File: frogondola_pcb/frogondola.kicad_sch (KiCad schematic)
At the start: 148 parts, among them J1 Conn_01x04_Pin, J10 Conn_01x01_Pin, J2 USB_C_Receptacle_USB2.0_14P, J3 Conn_01x01_Pin, J4 Conn_01x01_Pin, J5 Conn_01x01_Pin, J6 Conn_01x01_Pin, J7 Conn_01x01_Pin, J8 Conn_01x01_Pin, J9 Conn_01x01_Pin, SW1 SW_DPST_x2, SW2 SW_DPST_x2, U1 STM32F072CBTx, U2 TLV74318PDBVR, U3 XC6206PxxxMR, U4 PMW3360DM-T2QU, U5 SRV05-4

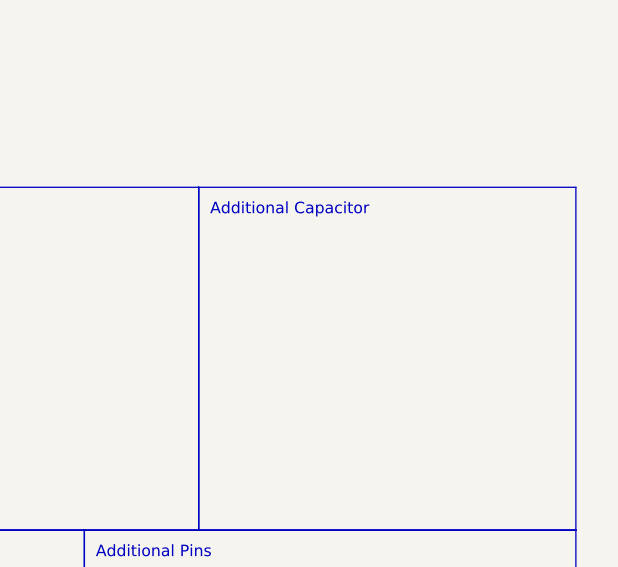
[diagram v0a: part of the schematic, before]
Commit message: Adde L60 outline footprint from https://github.com/dededecline/SST60, will update license too.
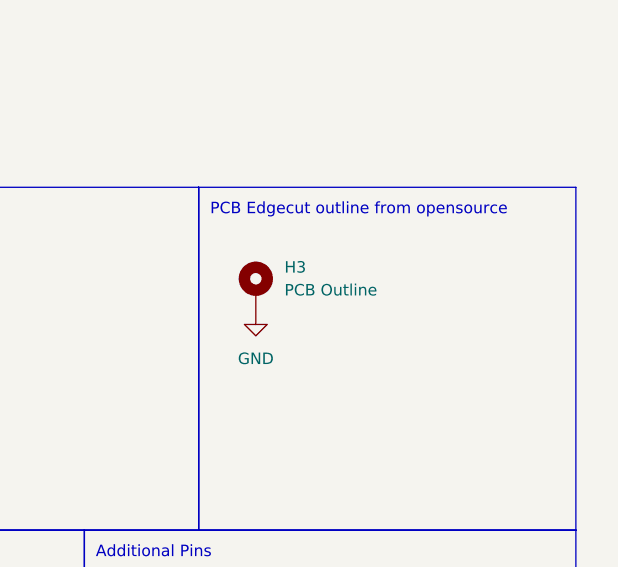
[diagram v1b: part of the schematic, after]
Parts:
- added H3: PCB Outline, pcb_outline:L60 Outline, symbol Mechanical:MountingHole_Pad
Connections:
- net GND: now also H3.1
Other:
- note added: "PCB Edgecut outline from opensource"
- note removed: "Additional Capacitor"
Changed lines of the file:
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@@
 		)
 	)
-	(text "Additional Capacitor"
+	(text "PCB Edgecut outline from opensource"
 		(exclude_from_sim no)
 		(at 367.03 63.5 0)
@@
 	)
 	(symbol
+		(lib_id "Mechanical:MountingHole_Pad")
+		(at 372.11 72.39 0)
+		(unit 1)
+		(exclude_from_sim no)
+		(in_bom yes)
+		(on_board yes)
+		(dnp no)
+		(fields_autoplaced yes)
+		(property "Reference" "H3"
+			(at 375.285 69.8499 0)
+			(effects
+				(font
+					(size 1.27 1.27)
+				)
+				(justify left)
+			)
+		)
+		(property "Value" "PCB Outline"
+			(at 375.285 72.3899 0)
+			(effects
+				(font
+					(size 1.27 1.27)
+				)
+				(justify left)
+			)
+		)
+		(property "Footprint" "pcb_outline:L60 Outline"
+			(at 372.11 72.39 0)
+			(effects
+				(font
+					(size 1.27 1.27)
+				)
+				(hide yes)
+			)
+		)
+		(property "Datasheet" "~"
+			(at 372.11 72.39 0)
+			(effects
+				(font
+					(size 1.27 1.27)
+				)
+				(hide yes)
+			)
+		)
+		(property "Description" ""
+			(at 372.11 72.39 0)
+			(effects
+				(font
+					(size 1.27 1.27)
+				)
+				(hide yes)
+			)
+		)
+		(pin "1"
+		)
+		(instances
+			(project "frogondola"
+				(path "/08852bcd-680f-4be6-8af1-42651f3c0f44"
+					(reference "H3")
+					(unit 1)
+				)
+			)
+		)
+	)
+	(symbol
 		(lib_id "Device:D")
 		(at 303.53 54.61 90)
@@
 					(unit 1)
 				)
+			)
+		)
+	)
+	(symbol
+		(lib_id "power:GND")
+		(at 372.11 74.93 0)
+		(unit 1)
+		(exclude_from_sim no)
+		(in_bom yes)
+		(on_board yes)
+		(dnp no)
+		(fields_autoplaced yes)
+		(property "Reference" "#PWR027"
+			(at 372.11 81.28 0)
+			(effects
+				(font
+					(size 1.27 1.27)
+				)
+				(hide yes)
+			)
+		)
+		(property "Value" "GND"
+			(at 372.11 80.01 0)
+			(effects
+				(font
+					(size 1.27 1.27)
+				)
+			)
+		)
+		(property "Footprint" ""
+			(at 372.11 74.93 0)
+			(effects
+				(font
+					(size 1.27 1.27)
+				)
+				(hide yes)
+			)
+		)
+		(property "Datasheet" ""
+			(at 372.11 74.93 0)
+			(effects
+				(font
+					(size 1.27 1.27)
+				)
+				(hide yes)
+			)
+		)
+		(property "Description" "Power symbol creates a global label with name \"GND\" , ground"
+			(at 372.11 74.93 0)
+			(effects
+				(font
+					(size 1.27 1.27)
+				)
+				(hide yes)
+			)
+		)
+		(pin "1"
+		)
+		(instances
+			(project ""
+				(path "/08852bcd-680f-4be6-8af1-42651f3c0f44"
+					(reference "#PWR027")
+					(unit 1)
+				)

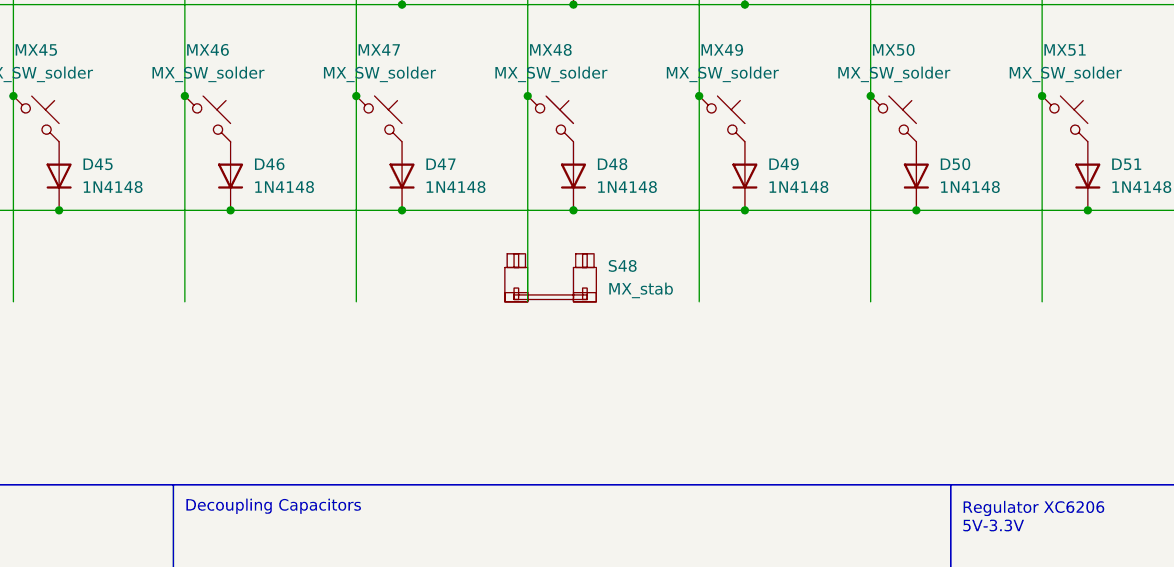
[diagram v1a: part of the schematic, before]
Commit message: updated pcb matrix & route.
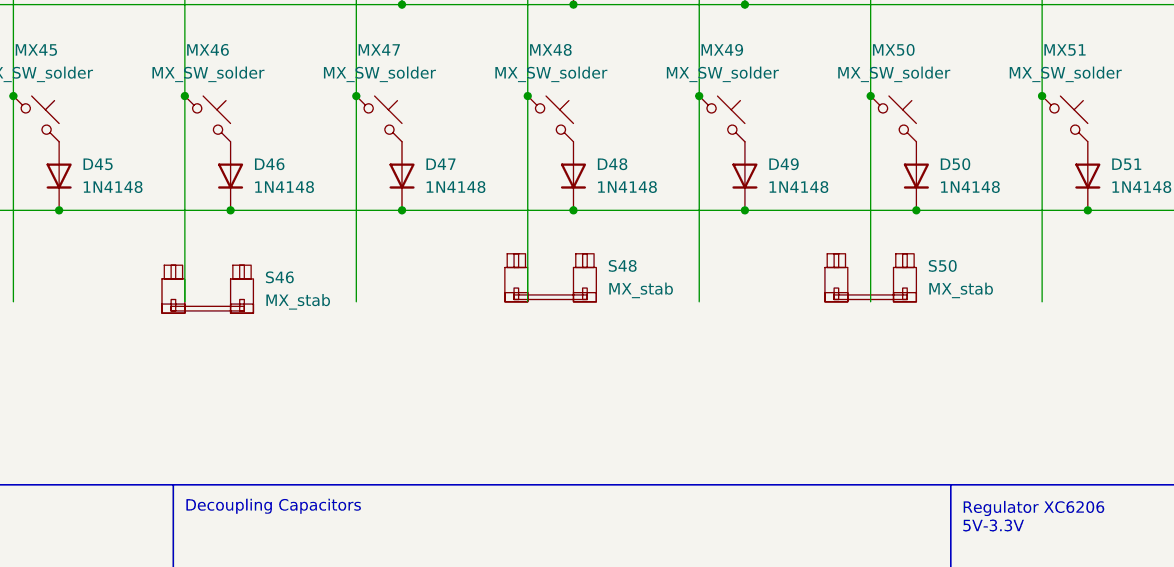
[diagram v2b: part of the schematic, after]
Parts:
- added S46, S50: MX_stab, PCM_marbastlib-mx:STAB_MX_P_3u, symbol PCM_marbastlib-mx:MX_stab
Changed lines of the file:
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@@
 	)
 	(symbol
+		(lib_id "PCM_marbastlib-mx:MX_stab")
+		(at 203.2 157.48 0)
+		(unit 1)
+		(exclude_from_sim no)
+		(in_bom yes)
+		(on_board yes)
+		(dnp no)
+		(fields_autoplaced yes)
+		(property "Reference" "S50"
+			(at 209.55 156.0829 0)
+			(effects
+				(font
+					(size 1.27 1.27)
+				)
+				(justify left)
+			)
+		)
+		(property "Value" "MX_stab"
+			(at 209.55 158.6229 0)
+			(effects
+				(font
+					(size 1.27 1.27)
+				)
+				(justify left)
+			)
+		)
+		(property "Footprint" "PCM_marbastlib-mx:STAB_MX_P_3u"
+			(at 203.2 157.48 0)
+			(effects
+				(font
+					(size 1.27 1.27)
+				)
+				(hide yes)
+			)
+		)
+		(property "Datasheet" ""
+			(at 203.2 157.48 0)
+			(effects
+				(font
+					(size 1.27 1.27)
+				)
+				(hide yes)
+			)
+		)
+		(property "Description" "Cherry MX-style stabilizer"
+			(at 203.2 157.48 0)
+			(effects
+				(font
+					(size 1.27 1.27)
+				)
+				(hide yes)
+			)
+		)
+		(instances
+			(project "frogondola"
+				(path "/08852bcd-680f-4be6-8af1-42651f3c0f44"
+					(reference "S50")
+					(unit 1)
+				)
+			)
+		)
+	)
+	(symbol
 		(lib_id "PCM_marbastlib-mx:MX_SW_solder")
 		(at 262.89 139.7 0)
@@
 					(unit 1)
 				)
+			)
+		)
+	)
+	(symbol
+		(lib_id "PCM_marbastlib-mx:MX_stab")
+		(at 129.54 158.75 0)
+		(unit 1)
+		(exclude_from_sim no)
+		(in_bom yes)
+		(on_board yes)
+		(dnp no)
+		(fields_autoplaced yes)
+		(property "Reference" "S46"
+			(at 135.89 157.3529 0)
+			(effects
+				(font
+					(size 1.27 1.27)
+				)
+				(justify left)
+			)
+		)
+		(property "Value" "MX_stab"
+			(at 135.89 159.8929 0)
+			(effects
+				(font
+					(size 1.27 1.27)
+				)
+				(justify left)
+			)
+		)
+		(property "Footprint" "PCM_marbastlib-mx:STAB_MX_P_3u"
+			(at 129.54 158.75 0)
+			(effects
+				(font
+					(size 1.27 1.27)
+				)
+				(hide yes)
+			)
+		)
+		(property "Datasheet" ""
+			(at 129.54 158.75 0)
+			(effects
+				(font
+					(size 1.27 1.27)
+				)
+				(hide yes)
+			)
+		)
+		(property "Description" "Cherry MX-style stabilizer"
+			(at 129.54 158.75 0)
+			(effects
+				(font
+					(size 1.27 1.27)
+				)
+				(hide yes)
+			)
+		)
+		(instances
+			(project "frogondola"
+				(path "/08852bcd-680f-4be6-8af1-42651f3c0f44"
+					(reference "S46")
+					(unit 1)
+				)

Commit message: Almost done!
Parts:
- C7: value C4_1uF -> C7_1uF
- J10, J7, J8, J9: footprint TestPoint:TestPoint_Pad_1.5x1.5mm -> TestPoint:TestPoint_THTPad_1.5x1.5mm_Drill0.7mm
- J2: MPN (none) -> C2894897
- R2: value R3_39R -> R2_39R
- R3, R5: value R1_10k -> R3_10k
- R4: value R2_10k -> R4_10k
- R6: value R5_5.1k -> R6_5.1k
- R7: value R6_5.1k -> R7_5.1k
- SW1, SW2: MPN (none) -> C318884
- U1: MPN (none) -> C81720
- U2: MPN (none) -> C485152
- U3: MPN (none) -> C5148692
- U5: MPN (none) -> C7420376
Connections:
- net ADD4 is gone; now on net ExNSS: J7.1 (Pin_1)
- net ADD5 is gone; now on net ExSCK: J8.1 (Pin_1)
- net ADD6 is gone; now on net ExMISO: J9.1 (Pin_1)
- net ADD7 is gone; now on net ExMOSI: J10.1 (Pin_1)
- net ADD0: now also U1.19 (PB1)
- net ADD1: now also U1.20 (PB2)
- net ADD2: now also U1.18 (PB0)
- net ADD3: now also U1.21 (PB10)
- net COL0: now also U1.43 (PB7)
- net COL1: now also U1.42 (PB6)
- net COL10: now also U1.6 (PF1)
- net COL11: now also U1.5 (PF0)
- net COL12: now also U1.4 (PC15)
- net COL13: now also U1.3 (PC14)
- net COL14: now also U1.2 (PC13)
- net COL2: now also U1.41 (PB5)
- net COL3: now also U1.40 (PB4)
- net COL4: now also U1.39 (PB3)
- net COL5: now also U1.38 (PA15)
- net COL6: now also U1.37 (PA14)
- net COL7: now also U1.34 (PA13)
- net COL8: now also U1.11 (PA1)
- net COL9: now also U1.10 (PA0)
- net ROW0: now also U1.31 (PA10)
- net ROW1: now also U1.30 (PA9)
- net ROW2: now also U1.29 (PA8)
- net ROW3: now also U1.12 (PA2)
- net ROW4: now also U1.13 (PA3)
- net ExNSS: now reaches U1.25 (PB12)
- net ExSCK: now reaches U1.26 (PB13)
- net ExMISO: now reaches U1.27 (PB14)
- net ExMOSI: now reaches U1.28 (PB15)
- no-connect marks 6 -> 9
